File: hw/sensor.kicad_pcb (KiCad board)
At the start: 2 copper layers, 50 x 50 mm, 35 parts, among them P2 CONN_01X03, P3 CONN_01X04, P4 CONN_01X05, U1 0868AT43A0020, U2 0896FB15A0100, U3 AT86RF212B, U4 ATSAML21E18B, U5 STLQ015, U6 BMP280, U7 TSL25711, U8 HTU21D, Y1 ECS-160-10-37-RWM-TR

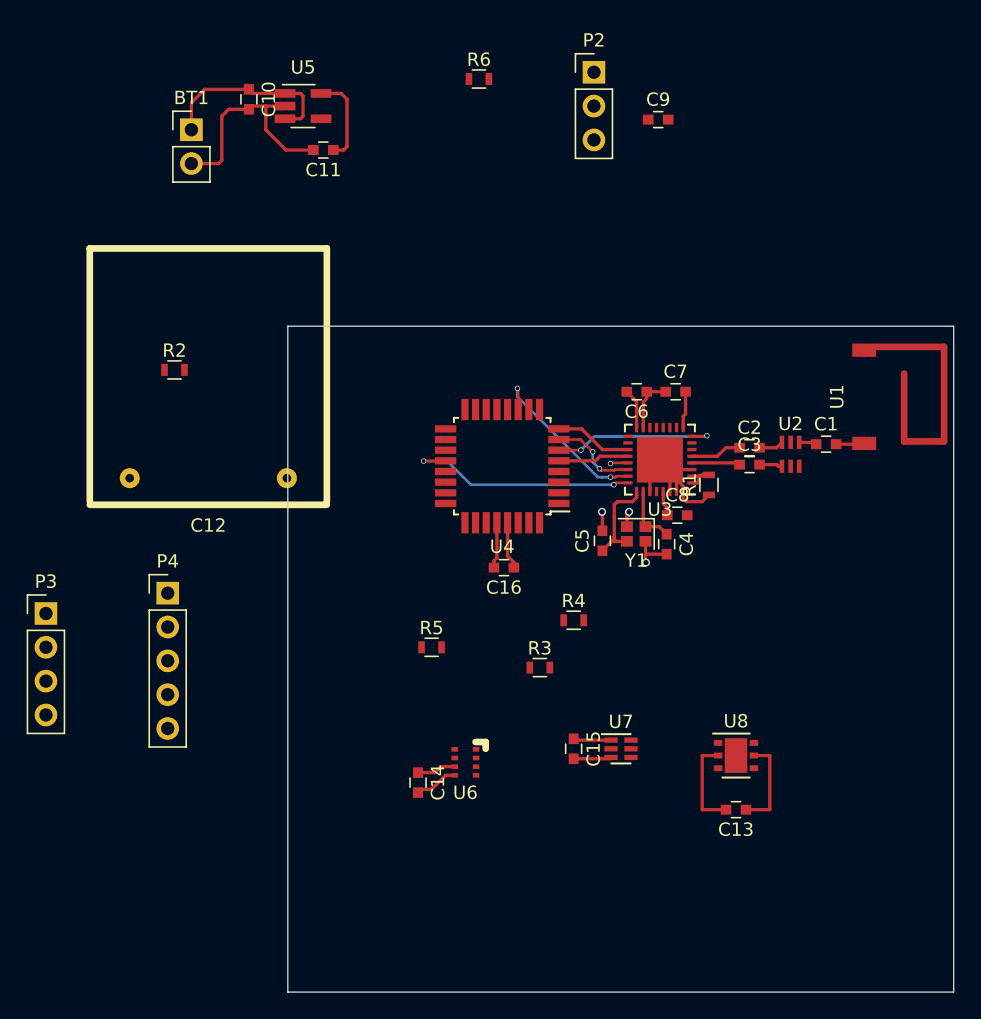
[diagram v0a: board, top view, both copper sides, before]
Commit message: complete routing
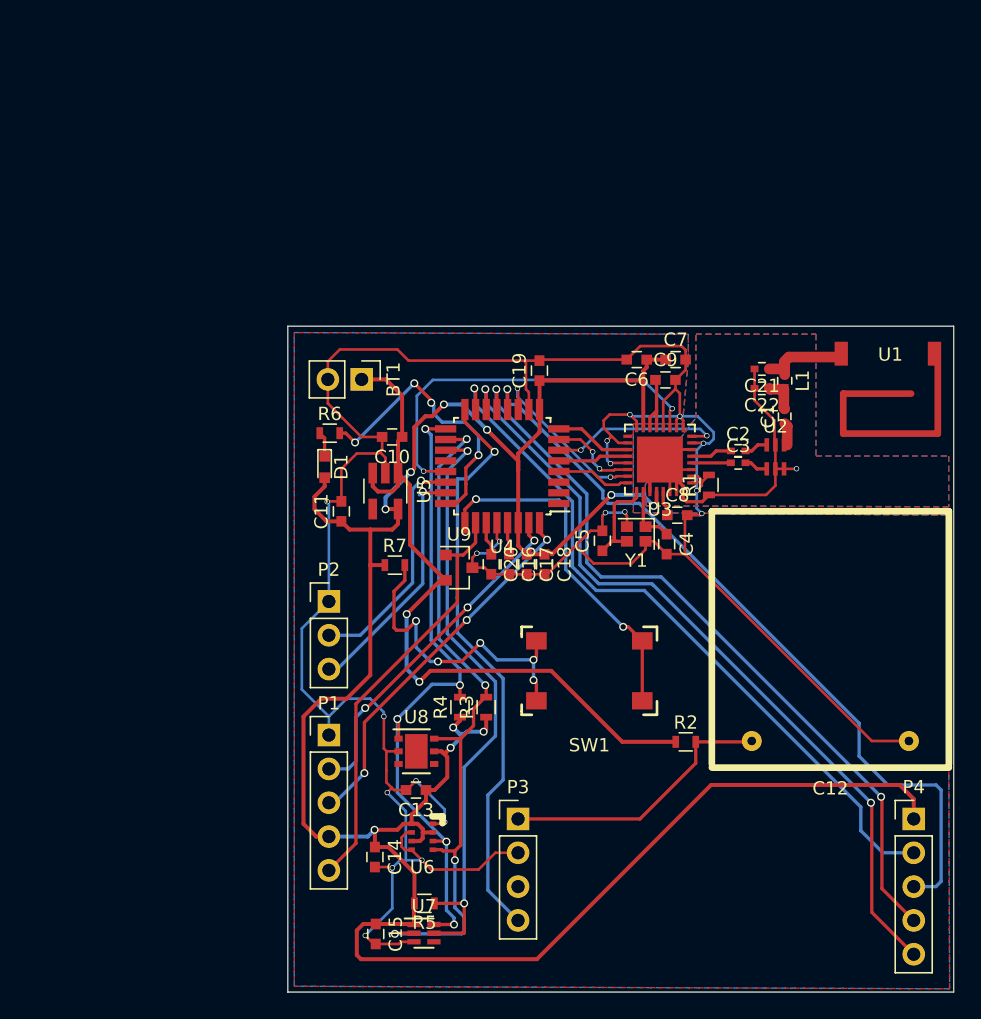
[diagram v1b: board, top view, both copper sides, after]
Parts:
- added C17: 10uF, Capacitors_SMD:C_0603, F.Cu at (152.9, 127.9)
- added C18: 100nF, Capacitors_SMD:C_0603, F.Cu at (154.3, 127.9)
- added C19: 100nF, Capacitors_SMD:C_0603, F.Cu at (153.9, 113.3)
- added C20: 1uF, Capacitors_SMD:C_0603, F.Cu at (150.3, 127.9)
- added C21: 0.3pF, Capacitors_SMD:C_0402, F.Cu at (170.6, 113.2)
- added C22: 3.9pF, Capacitors_SMD:C_0402, F.Cu at (170.6, 114.7)
- added D1: LED_Small, LEDs:LED_0603, F.Cu at (137.8, 120.6)
- added L1: 18nH, Resistors_SMD:R_0402, F.Cu at (172.3, 114.1)
- added P1: CONN_01X05, Pin_Headers:Pin_Header_Straight_1x05_Pitch2.54mm, F.Cu at (138.1, 140.7)
- added R7: 22k, Resistors_SMD:R_0603, F.Cu at (143.0, 127.9)
- added SW1: DTSM-61N, custom:DTSM-61N, F.Cu at (157.6, 135.9)
- added U9: MIC1815, TO_SOT_Packages_SMD:SOT-23, F.Cu at (147.9, 128.1)
- C1, C2, C3: footprint Capacitors_SMD:C_0603 -> Capacitors_SMD:C_0402
- R6: value 10k -> 330
- moved P4 58.5 mm to (182.0, 147.0)
- moved C12 50.7 mm to (175.7, 141.1)
- moved R2 47.5 mm to (164.9, 141.2)
- moved P2 44.4 mm to (138.1, 130.7)
- moved P3 38.7 mm to (152.3, 147.0)
- moved U5 29.6 mm to (142.3, 122.4), turned to 270 degrees
- moved R6 28.9 mm to (138.1, 118.0)
- moved C10 27.5 mm to (142.8, 118.3), turned to 180 degrees
- moved C11 27.2 mm to (139.0, 123.9), turned to 90 degrees
- moved C13 24.1 mm to (144.6, 144.8)
- moved U8 24.0 mm to (144.7, 141.9)
- moved BT1 22.7 mm to (140.5, 114.0), turned to 270 degrees
- moved C15 20.4 mm to (141.6, 155.6)
- moved U7 20.3 mm to (145.2, 155.6)
- moved C9 19.6 mm to (163.4, 114.0)
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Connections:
- P2 pad 1: Net-(P2-Pad1) -> GNDD
- P2 pad 3: GNDD -> Net-(P2-Pad3)
- R6 pad 1: Net-(R6-Pad1) -> Net-(D1-Pad1)
- R6 pad 2: +3V3 -> Net-(R6-Pad2)
- U1 pad 1: Net-(C1-Pad2) -> Net-(C21-Pad1)
- U4 pad 20: /Radio/RADIO_IRQ -> (no net)
- U4 pad 22: Net-(P2-Pad1) -> Net-(P2-Pad2)
- U4 pad 23: Net-(P2-Pad2) -> Net-(P2-Pad3)
- U4 pad 24: (no net) -> Net-(R6-Pad2)
- U4 pad 25: (no net) -> Net-(SW1-Pad3)
- U4 pad 26: Net-(R6-Pad1) -> RESET
- U4 pad 27: (no net) -> Net-(C20-Pad1)
- U4 pad 31: (no net) -> Net-(P1-Pad2)
- U4 pad 32: (no net) -> Net-(P1-Pad3)
- U4 pad 4: (no net) -> /Radio/RADIO_IRQ
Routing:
- net GNDD: track 48.9 -> 215.7 mm, vias 4 -> 19
- net +3V3: track 23.9 -> 189.0 mm, vias 0 -> 10
- net /cpu/CO2_RDY: track 0.00 -> 59.7 mm, vias 0 -> 2
- net /sensors/CO2_RXD: track 0.00 -> 58.1 mm, vias 0 -> 1
- net /sensors/CO2_TXD: track 0.00 -> 57.1 mm, vias 0 -> 2
- net /cpu/CO2_EN_VBB: track 0.00 -> 53.6 mm, vias 0 -> 1
- net /cpu/I2C_SCL: track 0.00 -> 52.6 mm, vias 0 -> 4
- net /cpu/I2C_SDA: track 0.00 -> 49.9 mm, vias 0 -> 5
- net /cpu/LIGHT_IRQ: track 0.00 -> 45.5 mm, vias 0 -> 2
- net /cpu/CO2_RESET: track 0.00 -> 43.8 mm, vias 0 -> 1
- net +BATT: track 14.0 -> 54.5 mm, vias 0 -> 2
- net RESET: track 0.00 -> 31.8 mm
- net /cpu/RADIO_SLP_TR: track 0.00 -> 29.6 mm, vias 0 -> 2
- net Net-(P1-Pad3): track 0.00 -> 28.3 mm, vias 0 -> 3
- net Net-(SW1-Pad3): track 0.00 -> 26.3 mm, vias 0 -> 2
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- added copper zone on B.Cu, net GNDA
- added copper zone on F.Cu, net GNDA
- added copper zone on B.Cu, net GNDD
- added copper zone on F.Cu, net GNDD
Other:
- net class 50ohm added: clearance 0.2, trace_width 0.8, via_dia 0.6, via_drill 0.4
- net class Power added: clearance 0.2, trace_width 0.3, via_dia 0.6, via_drill 0.4

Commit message: add battery voltage to adc and thicker traces for radio
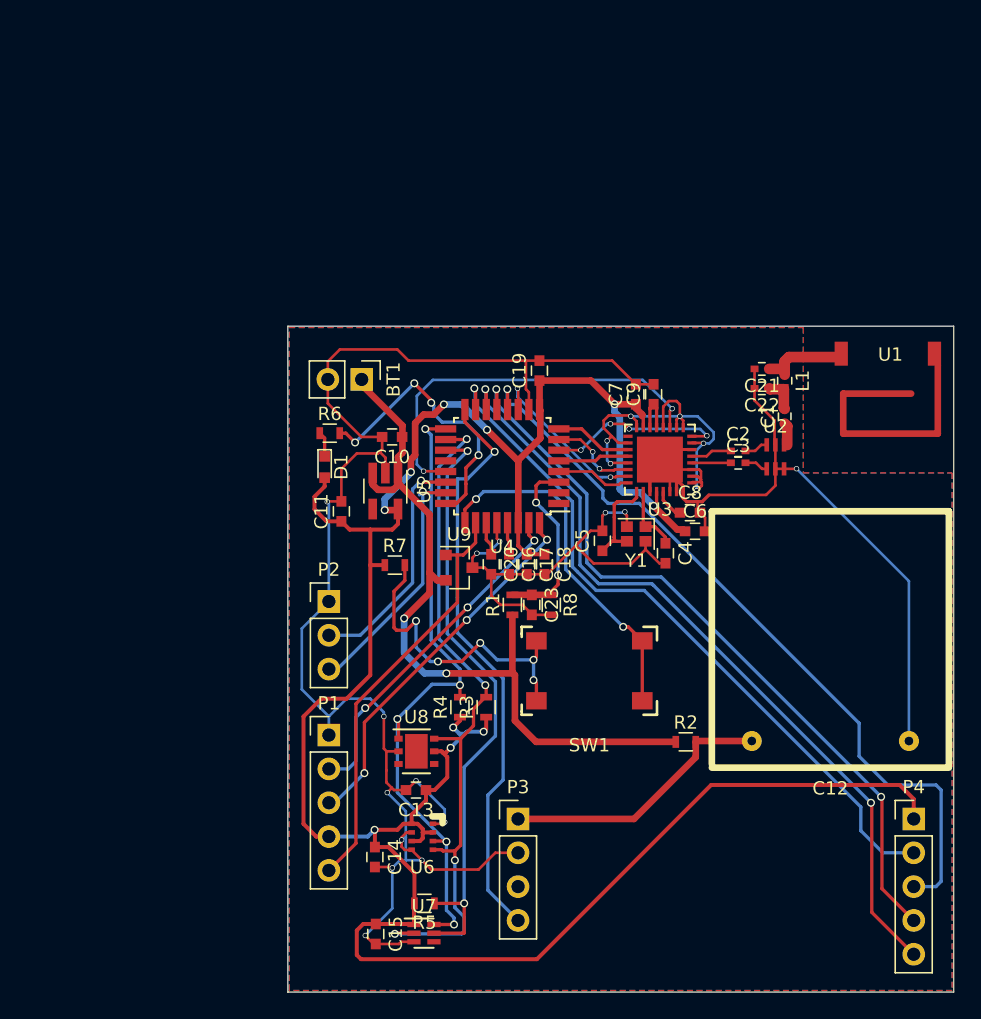
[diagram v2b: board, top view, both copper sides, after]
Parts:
- added C23: C_Small, Capacitors_SMD:C_0603, F.Cu at (153.3, 130.9)
- added R8: R_Small, Resistors_SMD:R_0603, F.Cu at (154.8, 130.9)
- R1: value 0 -> R_Small
- moved R1 17.3 mm to (151.9, 130.9)
- moved C6 13.6 mm to (165.6, 125.4), turned to 0 degrees
- moved C7 3.96 mm to (161.1, 115.1), turned to 90 degrees
- moved C9 1.40 mm to (162.5, 115.1), turned to 90 degrees
- moved C8 0.97 mm to (165.2, 124.0)
- moved C4 0.69 mm to (163.4, 127.1)
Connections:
- C21 pad 2: GNDA -> GNDD
- C22 pad 2: GNDA -> GNDD
- R1 pad 1: GNDA -> +BATT
- R1 pad 2: GNDD -> Net-(C23-Pad1)
- U2 pad 2: GNDA -> GNDD
- U2 pad 5: GNDA -> GNDD
- U2 pad 6: GNDA -> GNDD
- U3 pad 27: GNDA -> GNDD
- U3 pad 3: GNDA -> GNDD
- U3 pad 30: GNDA -> GNDD
- U3 pad 31: GNDA -> GNDD
- U3 pad 32: GNDA -> GNDD
- U3 pad 33: GNDA -> GNDD
- U3 pad 6: GNDA -> GNDD
- U4 pad 3: (no net) -> Net-(C23-Pad1)
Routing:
- net GNDA: track 37.1 -> 0.00 mm, vias 1 -> 0
- net GNDD: track 215.7 -> 249.9 mm, vias 19 -> 20
- net Net-(C23-Pad1): track 0.00 -> 15.3 mm, vias 0 -> 2
- net +BATT: track 54.5 -> 58.8 mm
- net +3V3: track 189.0 -> 186.8 mm
- net Net-(C1-Pad1): track 1.76 -> 3.37 mm
- net Net-(C9-Pad1): track 5.09 -> 4.42 mm
- net Net-(SW1-Pad3): track 26.3 -> 26.9 mm
- net /Radio/RESET_RF: track 13.2 -> 13.5 mm, vias 2 -> 4
- removed copper zone on B.Cu, net GNDA
- removed copper zone on F.Cu, net GNDA
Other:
- net class Power removed

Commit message: added a lot of stiching
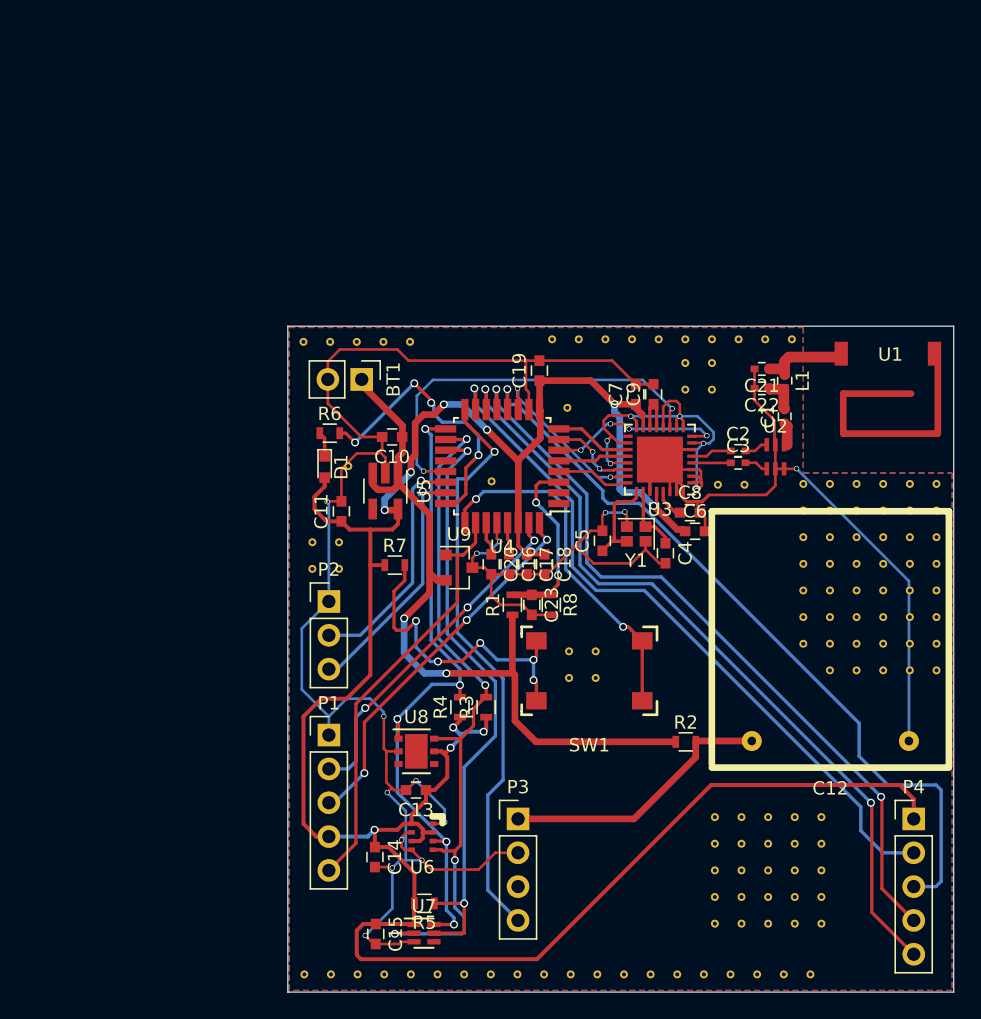
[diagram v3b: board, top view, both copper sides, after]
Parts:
- added REF**: STICH, custom:STICH, F.Cu at (144.2, 111.2)
- added REF**: STICH, custom:STICH, F.Cu at (166.8, 112.8)
- added REF**: STICH, custom:STICH, F.Cu at (162.2, 158.7)
- added REF**: STICH, custom:STICH, F.Cu at (160.2, 158.7)
- added REF**: STICH, custom:STICH, F.Cu at (158.2, 158.7)
- added REF**: STICH, custom:STICH, F.Cu at (156.2, 158.7)
- added REF**: STICH, custom:STICH, F.Cu at (154.2, 158.7)
- added REF**: STICH, custom:STICH, F.Cu at (152.2, 158.7)
- added REF**: STICH, custom:STICH, F.Cu at (150.2, 158.7)
- added REF**: STICH, custom:STICH, F.Cu at (148.2, 158.7)
- added REF**: STICH, custom:STICH, F.Cu at (146.2, 158.7)
- added REF**: STICH, custom:STICH, F.Cu at (144.2, 158.7)
- added REF**: STICH, custom:STICH, F.Cu at (164.8, 112.8)
- added REF**: STICH, custom:STICH, F.Cu at (142.2, 158.7)
- added REF**: STICH, custom:STICH, F.Cu at (140.2, 158.7)
- added REF**: STICH, custom:STICH, F.Cu at (138.2, 158.7)
- added REF**: STICH, custom:STICH, F.Cu at (136.2, 158.7)
- added REF**: STICH, custom:STICH, F.Cu at (172.8, 111.0)
- added REF**: STICH, custom:STICH, F.Cu at (170.8, 111.0)
- added REF**: STICH, custom:STICH, F.Cu at (168.8, 111.0)
- added REF**: STICH, custom:STICH, F.Cu at (166.8, 111.0)
- added REF**: STICH, custom:STICH, F.Cu at (164.8, 111.0)
- added REF**: STICH, custom:STICH, F.Cu at (162.8, 111.0)
- added REF**: STICH, custom:STICH, F.Cu at (169.3, 121.9)
- added REF**: STICH, custom:STICH, F.Cu at (160.8, 111.0)
- added REF**: STICH, custom:STICH, F.Cu at (158.8, 111.0)
- added REF**: STICH, custom:STICH, F.Cu at (156.8, 111.0)
- added REF**: STICH, custom:STICH, F.Cu at (154.8, 111.0)
- added REF**: STICH, custom:STICH, F.Cu at (173.7, 121.8)
- added REF**: STICH, custom:STICH, F.Cu at (167.3, 121.9)
- added REF**: STICH, custom:STICH, F.Cu at (183.7, 135.8)
- added REF**: STICH, custom:STICH, F.Cu at (181.7, 135.8)
- added REF**: STICH, custom:STICH, F.Cu at (179.7, 135.8)
- added REF**: STICH, custom:STICH, F.Cu at (177.7, 135.8)
- added REF**: STICH, custom:STICH, F.Cu at (175.7, 135.8)
- added REF**: STICH, custom:STICH, F.Cu at (183.7, 133.8)
- added REF**: STICH, custom:STICH, F.Cu at (142.2, 111.2)
- added REF**: STICH, custom:STICH, F.Cu at (181.7, 133.8)
- added REF**: STICH, custom:STICH, F.Cu at (179.7, 133.8)
- added REF**: STICH, custom:STICH, F.Cu at (177.7, 133.8)
- added REF**: STICH, custom:STICH, F.Cu at (175.7, 133.8)
- added REF**: STICH, custom:STICH, F.Cu at (173.7, 133.8)
- added REF**: STICH, custom:STICH, F.Cu at (183.7, 131.8)
- added REF**: STICH, custom:STICH, F.Cu at (181.7, 131.8)
- added REF**: STICH, custom:STICH, F.Cu at (179.7, 131.8)
- added REF**: STICH, custom:STICH, F.Cu at (177.7, 131.8)
- added REF**: STICH, custom:STICH, F.Cu at (175.7, 131.8)
- added REF**: STICH, custom:STICH, F.Cu at (140.2, 111.2)
- added REF**: STICH, custom:STICH, F.Cu at (173.7, 131.8)
- added REF**: STICH, custom:STICH, F.Cu at (183.7, 129.8)
- added REF**: STICH, custom:STICH, F.Cu at (181.7, 129.8)
- added REF**: STICH, custom:STICH, F.Cu at (179.7, 129.8)
- added REF**: STICH, custom:STICH, F.Cu at (177.7, 129.8)
- added REF**: STICH, custom:STICH, F.Cu at (175.7, 129.8)
- added REF**: STICH, custom:STICH, F.Cu at (173.7, 129.8)
- added REF**: STICH, custom:STICH, F.Cu at (183.7, 127.8)
- added REF**: STICH, custom:STICH, F.Cu at (181.7, 127.8)
- added REF**: STICH, custom:STICH, F.Cu at (179.7, 127.8)
- added REF**: STICH, custom:STICH, F.Cu at (138.2, 111.2)
- added REF**: STICH, custom:STICH, F.Cu at (177.7, 127.8)
- added REF**: STICH, custom:STICH, F.Cu at (175.7, 127.8)
- added REF**: STICH, custom:STICH, F.Cu at (173.7, 127.8)
- added REF**: STICH, custom:STICH, F.Cu at (183.7, 125.8)
- added REF**: STICH, custom:STICH, F.Cu at (181.7, 125.8)
- added REF**: STICH, custom:STICH, F.Cu at (179.7, 125.8)
- added REF**: STICH, custom:STICH, F.Cu at (177.7, 125.8)
- added REF**: STICH, custom:STICH, F.Cu at (175.7, 125.8)
- added REF**: STICH, custom:STICH, F.Cu at (173.7, 125.8)
- added REF**: STICH, custom:STICH, F.Cu at (183.7, 123.8)
- added REF**: STICH, custom:STICH, F.Cu at (136.2, 111.2)
- added REF**: STICH, custom:STICH, F.Cu at (181.7, 123.8)
- added REF**: STICH, custom:STICH, F.Cu at (179.7, 123.8)
- added REF**: STICH, custom:STICH, F.Cu at (177.7, 123.8)
- added REF**: STICH, custom:STICH, F.Cu at (175.7, 123.8)
- added REF**: STICH, custom:STICH, F.Cu at (173.7, 123.8)
- added REF**: STICH, custom:STICH, F.Cu at (183.7, 121.8)
- added REF**: STICH, custom:STICH, F.Cu at (181.7, 121.8)
- added REF**: STICH, custom:STICH, F.Cu at (179.7, 121.8)
- added REF**: STICH, custom:STICH, F.Cu at (177.7, 121.8)
- added REF**: STICH, custom:STICH, F.Cu at (175.7, 121.8)
- added REF**: STICH, custom:STICH, F.Cu at (139.5, 120.5)
- added REF**: STICH, custom:STICH, F.Cu at (138.8, 128.2)
- added REF**: STICH, custom:STICH, F.Cu at (136.8, 128.2)
- added REF**: STICH, custom:STICH, F.Cu at (138.8, 126.2)
- added REF**: STICH, custom:STICH, F.Cu at (136.8, 126.2)
- added REF**: STICH, custom:STICH, F.Cu at (158.1, 136.4)
- added REF**: STICH, custom:STICH, F.Cu at (156.1, 136.4)
- added REF**: STICH, custom:STICH, F.Cu at (158.1, 134.4)
- added REF**: STICH, custom:STICH, F.Cu at (156.1, 134.4)
- added REF**: STICH, custom:STICH, F.Cu at (175.1, 154.9)
- added REF**: STICH, custom:STICH, F.Cu at (173.1, 154.9)
- added REF**: STICH, custom:STICH, F.Cu at (156.0, 116.1)
- added REF**: STICH, custom:STICH, F.Cu at (171.1, 154.9)
- added REF**: STICH, custom:STICH, F.Cu at (169.1, 154.9)
- added REF**: STICH, custom:STICH, F.Cu at (167.1, 154.9)
- added REF**: STICH, custom:STICH, F.Cu at (175.1, 152.9)
- added REF**: STICH, custom:STICH, F.Cu at (173.1, 152.9)
- added REF**: STICH, custom:STICH, F.Cu at (171.1, 152.9)
- added REF**: STICH, custom:STICH, F.Cu at (169.1, 152.9)
- added REF**: STICH, custom:STICH, F.Cu at (167.1, 152.9)
- added REF**: STICH, custom:STICH, F.Cu at (175.1, 150.9)
- added REF**: STICH, custom:STICH, F.Cu at (173.1, 150.9)
- added REF**: STICH, custom:STICH, F.Cu at (166.8, 114.8)
- added REF**: STICH, custom:STICH, F.Cu at (171.1, 150.9)
- added REF**: STICH, custom:STICH, F.Cu at (169.1, 150.9)
- added REF**: STICH, custom:STICH, F.Cu at (167.1, 150.9)
- added REF**: STICH, custom:STICH, F.Cu at (175.1, 148.9)
- added REF**: STICH, custom:STICH, F.Cu at (173.1, 148.9)
- added REF**: STICH, custom:STICH, F.Cu at (171.1, 148.9)
- added REF**: STICH, custom:STICH, F.Cu at (169.1, 148.9)
- added REF**: STICH, custom:STICH, F.Cu at (167.1, 148.9)
- added REF**: STICH, custom:STICH, F.Cu at (175.1, 146.9)
- added REF**: STICH, custom:STICH, F.Cu at (173.1, 146.9)
- added REF**: STICH, custom:STICH, F.Cu at (164.8, 114.8)
- added REF**: STICH, custom:STICH, F.Cu at (171.1, 146.9)
- added REF**: STICH, custom:STICH, F.Cu at (169.1, 146.9)
- added REF**: STICH, custom:STICH, F.Cu at (167.1, 146.9)
- added REF**: STICH, custom:STICH, F.Cu at (150.3, 121.7)
- added REF**: STICH, custom:STICH, F.Cu at (174.2, 158.7)
- added REF**: STICH, custom:STICH, F.Cu at (172.2, 158.7)
- added REF**: STICH, custom:STICH, F.Cu at (170.2, 158.7)
- added REF**: STICH, custom:STICH, F.Cu at (168.2, 158.7)
- added REF**: STICH, custom:STICH, F.Cu at (166.2, 158.7)
- added REF**: STICH, custom:STICH, F.Cu at (164.2, 158.7)
